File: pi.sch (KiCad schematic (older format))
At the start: 8 parts, among them J2 OLED, J3 OLED, J4 DAC BOARD, J5 DAC BOARD, J6 Hitachi HD44780, J7 POST, J8 POST

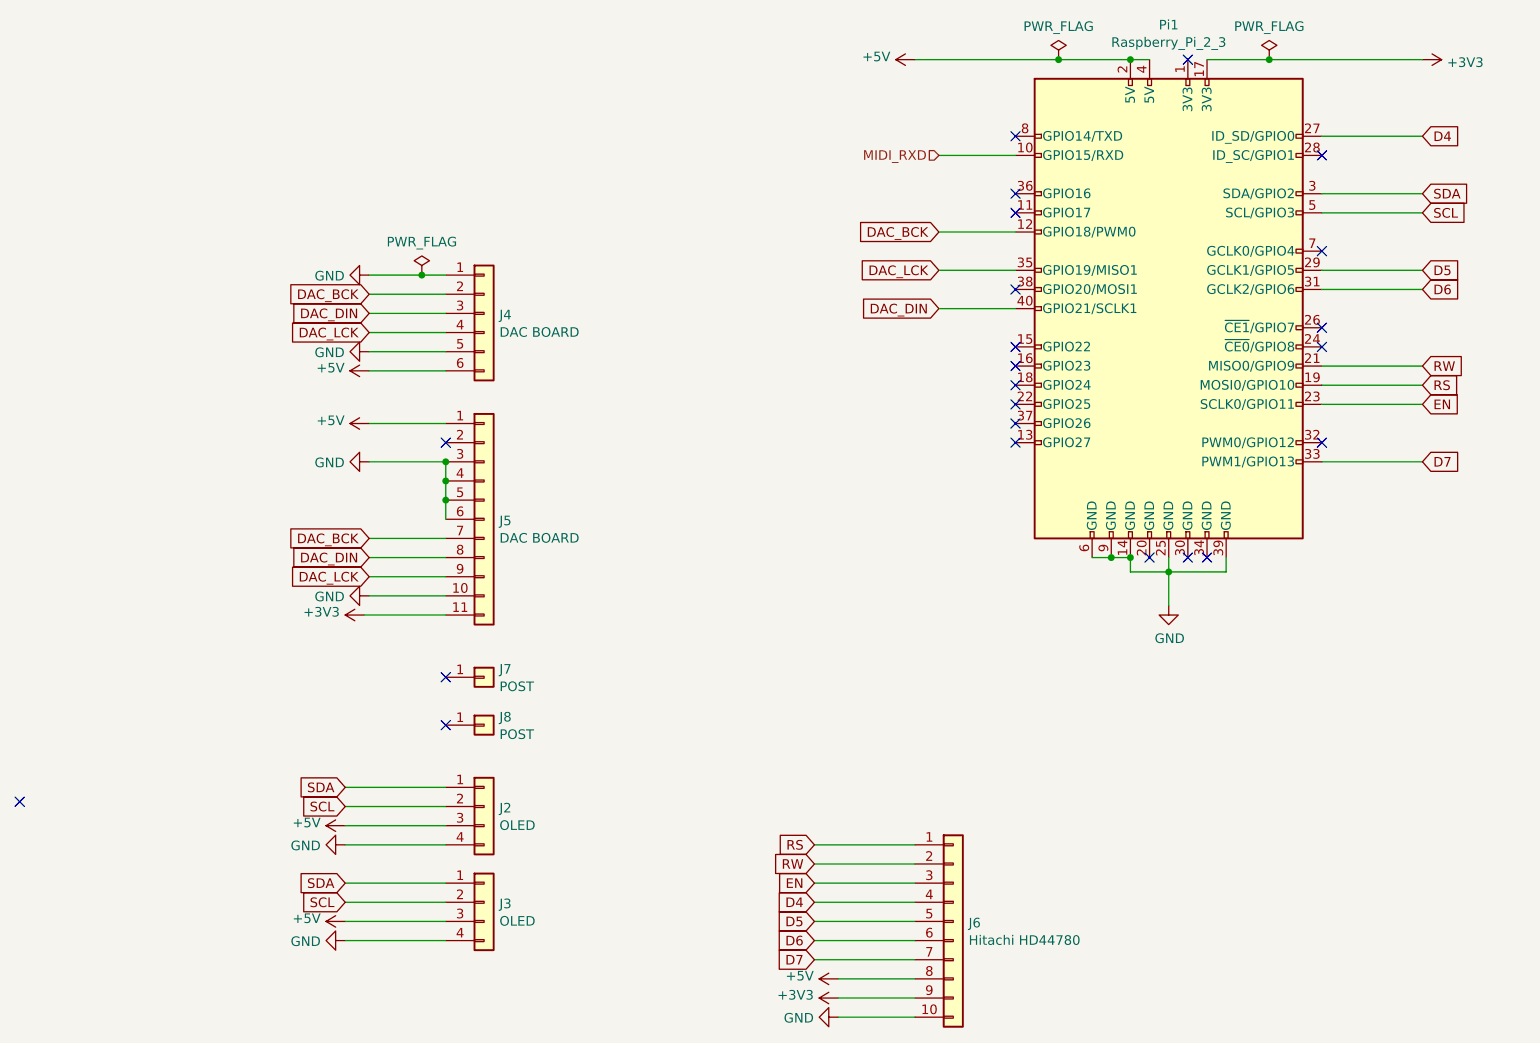
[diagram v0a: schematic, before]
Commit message: Version 1.6
1. Removed Hitachi 4bit version
2. Added new buttons from version 0.8 of the mt32-pi project
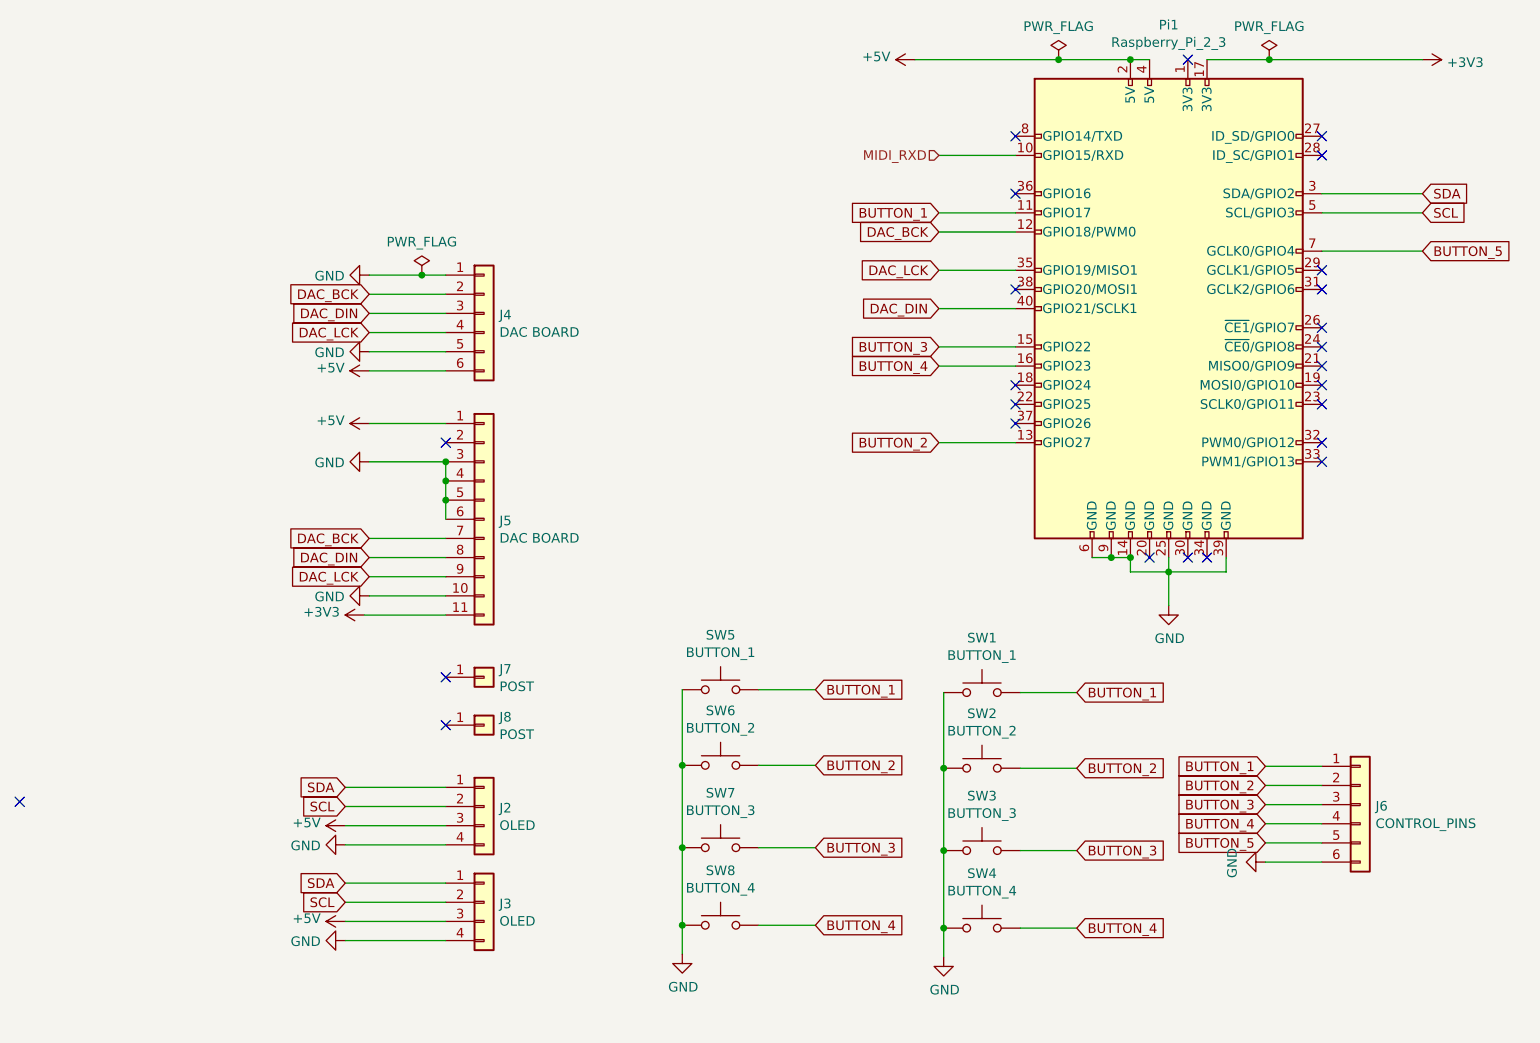
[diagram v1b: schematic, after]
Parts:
- removed J6: Hitachi HD44780, Connector_PinHeader_2.54mm:PinHeader_1x10_P2.54mm_Vertical, symbol Connector_Generic:Conn_01x10
- added J6: CONTROL_PINS, Connector_PinHeader_2.54mm:PinHeader_1x06_P2.54mm_Vertical, symbol Connector_Generic:Conn_01x06
- added SW1, SW5: BUTTON_1, Button_Switch_THT:SW_PUSH_6mm_SLIM, symbol Switch:SW_Push
- added SW2, SW6: BUTTON_2, Button_Switch_THT:SW_PUSH_6mm_SLIM, symbol Switch:SW_Push
- added SW3, SW7: BUTTON_3, Button_Switch_THT:SW_PUSH_6mm_SLIM, symbol Switch:SW_Push
- added SW4, SW8: BUTTON_4, Button_Switch_THT:SW_PUSH_6mm_SLIM, symbol Switch:SW_Push
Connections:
- net GND: now also J6.6 (Pin_6), SW1.1, SW2.1, SW3.1, SW4.1, SW5.1, SW6.1, SW7.1, SW8.1
- net BUTTON_1: now reaches Pi1.11 (GPIO17)
- net BUTTON_1: now also J6.1 (Pin_1), SW1.2, SW5.2
- net BUTTON_2: now reaches Pi1.13 (GPIO27)
- net BUTTON_2: now also J6.2 (Pin_2), SW2.2, SW6.2
- net BUTTON_3: now reaches Pi1.15 (GPIO22)
- net BUTTON_3: now also J6.3 (Pin_3), SW3.2, SW7.2
- net BUTTON_4: now reaches Pi1.16 (GPIO23)
- net BUTTON_4: now also J6.4 (Pin_4), SW4.2, SW8.2
- net BUTTON_5: now reaches Pi1.7 (GCLK0/GPIO4)
- net BUTTON_5: now also J6.5 (Pin_5)
- net D4: no longer names the net of Pi1.27 (ID_SD/GPIO0)
- net D5: no longer names the net of Pi1.29 (GCLK1/GPIO5)
- net D6: no longer names the net of Pi1.31 (GCLK2/GPIO6)
- net D7: no longer names the net of Pi1.33 (PWM1/GPIO13)
- net EN: no longer names the net of Pi1.23 (SCLK0/GPIO11)
- net RS: no longer names the net of Pi1.19 (MOSI0/GPIO10)
- net RW: no longer names the net of Pi1.21 (MISO0/GPIO9)
- no-connect marks 23 -> 25
